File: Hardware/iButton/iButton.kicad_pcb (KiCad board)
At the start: 2 copper layers, 15.8 x 24.3 mm, 29 parts, among them IC1 TSOP75338TR, J1 Conn_01x06, X1b1 PG-2.5-9.5-SM, X2b1 PG-2.5-8.0-SM, X3b1 PG-3.0-10.0-SM

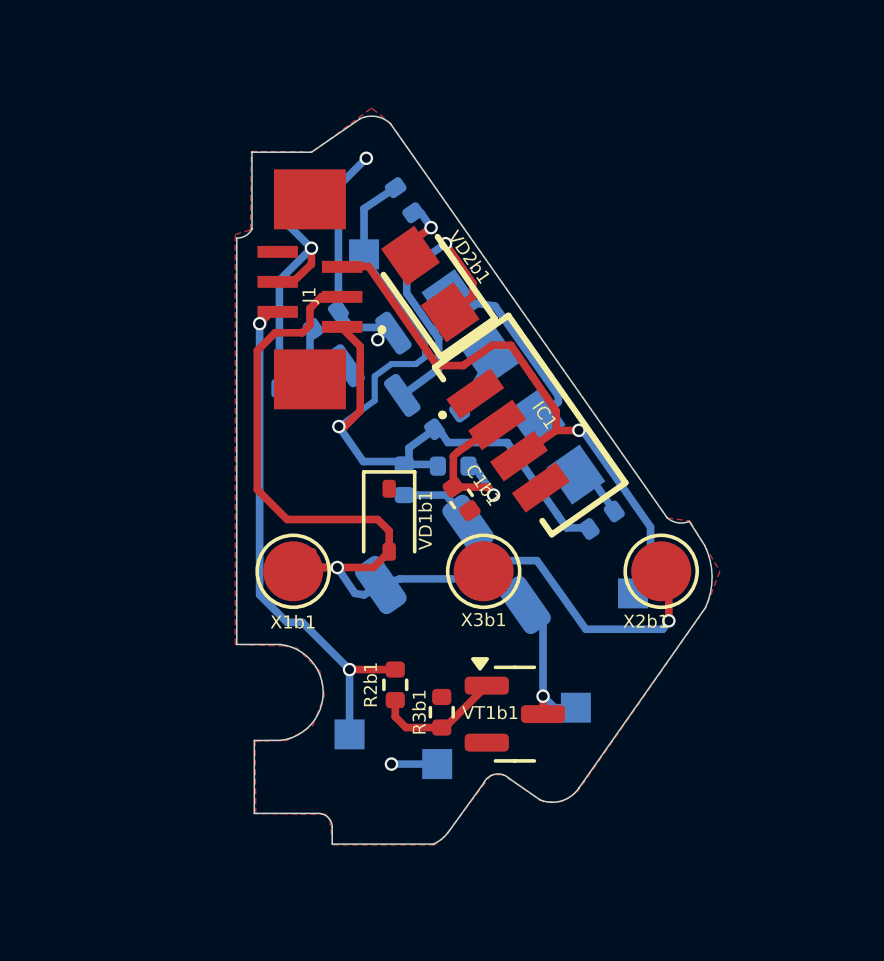
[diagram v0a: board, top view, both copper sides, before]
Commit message: PCB: Re layout the iBTN board
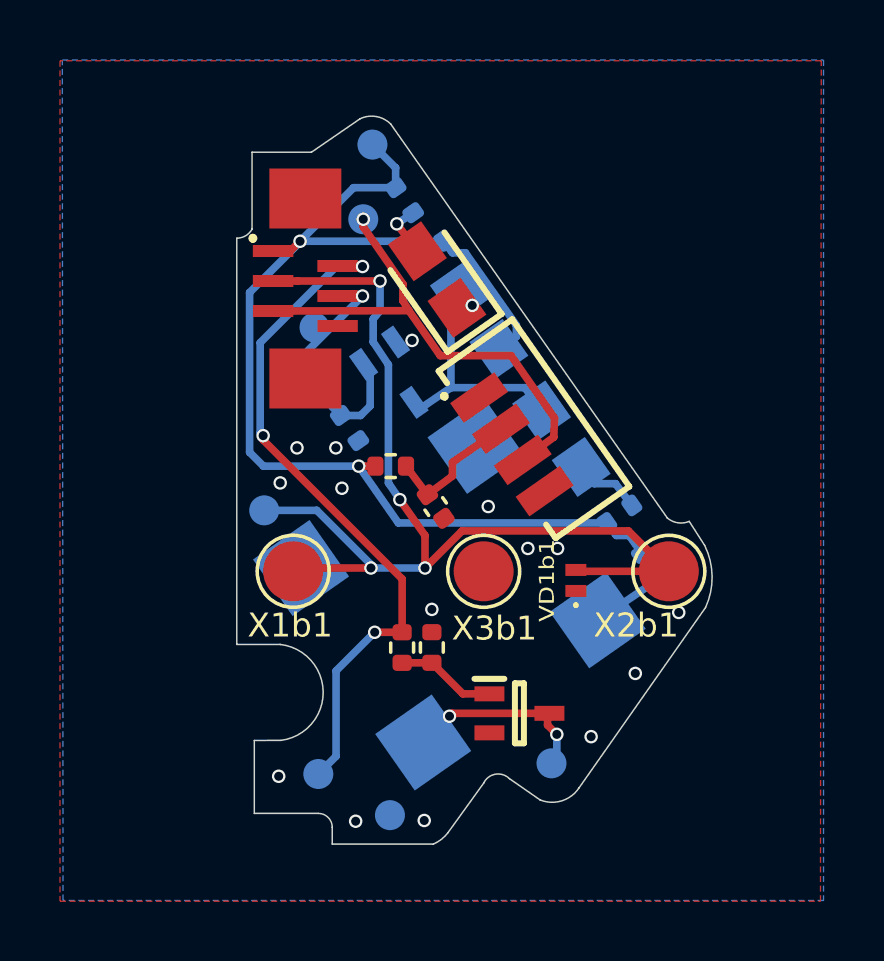
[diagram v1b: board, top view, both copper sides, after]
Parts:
- BA1b1: value SMD-5025-0340-12Ω -> MLT-8530; footprint Library:BUZ-SMD_3P-L5.0-W5.0-BL -> Library:MLT8530
- GND1, IR_RX1, IR_TX1, SPEAKER1, SPEAKER2, SYS1, iButton1: footprint TestPoint:TestPoint_Pad_1.0x1.0mm -> TestPoint:TestPoint_Pad_D1.0mm
- R7b1: moved to F.Cu
- VD1b1: value SD05_SOD323 -> D5V0H1B2LP-7B; footprint Diode_SMD:D_SOD-323 -> Library:D5V0H1B2LP7B
- VT1b1, VT2b1: footprint Package_TO_SOT_SMD:SOT-23 -> Library:SOT65P210X110-3N
- moved IR_RX1 15.4 mm to (162.5, 89.0)
- moved R1b1 8.70 mm to (172.0, 100.6), turned to -55 degrees
- moved VD1b1 6.54 mm to (169.5, 101.1), turned to 90 degrees
- moved R10b1 5.71 mm to (164.7, 90.0)
- moved IR_TX1 4.75 mm to (160.8, 92.6)
- moved R8b1 3.69 mm to (162.0, 96.0), turned to -55 degrees
- moved SYS1 3.67 mm to (162.8, 86.5)
- moved BA1b1 3.59 mm to (165.3, 101.5), turned to 35 degrees
- moved GND1 2.32 mm to (163.3, 108.9)
- moved iButton1 2.25 mm to (159.2, 98.7)
- moved R3b1 2.18 mm to (164.7, 103.3)
- moved R7b1 2.08 mm to (163.4, 97.3)
- moved SPEAKER1 2.02 mm to (168.7, 107.2)
- moved SPEAKER2 1.68 mm to (161.0, 107.5)
- moved R2b1 1.26 mm to (163.8, 103.3)
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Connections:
- BA1b1 pad 3: /iButton -> (no net)
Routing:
- net GND: track 9.80 -> 0.00 mm, vias 3 -> 15
- net Net-(VD2b1-K): track 17.9 -> 8.63 mm
- net SYS: track 27.6 -> 34.1 mm, vias 1 -> 2
- net /SPEAKER: track 17.4 -> 23.3 mm, vias 2 -> 3
- net /IR_TX: track 9.35 -> 4.95 mm
- net /IR_RX: track 20.5 -> 16.8 mm
- net Net-(VD4b1-A): track 2.15 -> 4.97 mm
- net Net-(BA1b1--): track 5.14 -> 6.41 mm, vias 1 -> 2
- net Net-(IC1-VS): track 5.66 -> 4.66 mm, vias 1 -> 0
- net Net-(VT1b1-G): track 4.33 -> 3.34 mm
- net Net-(VD3b1-A): track 1.79 -> 2.32 mm
- net Net-(VD2b1-A): track 2.34 -> 1.80 mm
- net /iButton: track 34.7 -> 34.9 mm, vias 2 -> 4
- added copper zone on B.Cu, net GND
